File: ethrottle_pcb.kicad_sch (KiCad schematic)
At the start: 52 parts, among them J1 ATM15-08PA-BM02, K1 DIP12-1C90-51x, U1 LM4040DBZ-5, U2 LM324, U3 LM324, U4 LM358_DFN

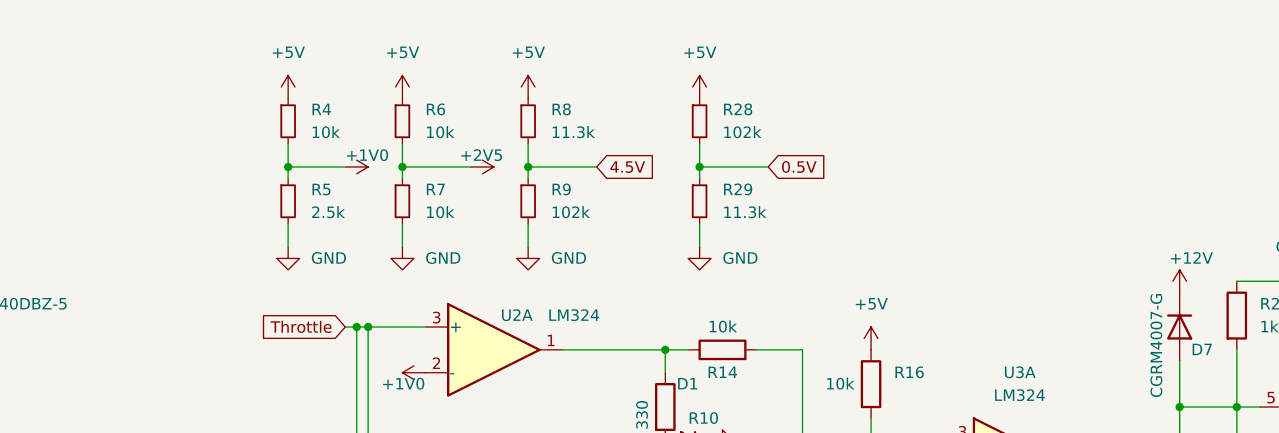
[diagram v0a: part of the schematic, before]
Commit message: add potentiometer
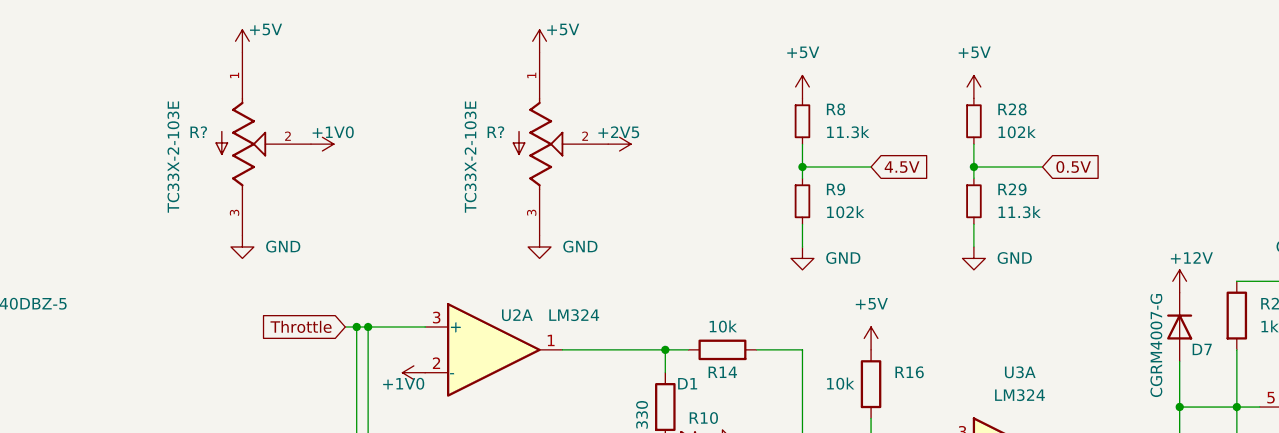
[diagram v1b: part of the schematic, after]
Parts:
- removed R4, R6, R7: 10k, Resistor_SMD:R_01005_0402Metric, symbol Device:R_Small
- removed R5: 2.5k, Resistor_SMD:R_01005_0402Metric, symbol Device:R_Small
- added R? (x2): TC33X-2-103E, TC33X-2-103E:TRIM_TC33X-2-103E, symbol TC33X-2-103E:TC33X-2-103E
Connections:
- net +1V0: now also R?.2
- net +2V5: now also R?.2
- net +5V: now also R?.1, R?.1
- net GND: now also R?.3, R?.3
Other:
- moved on the sheet: R28, R29, R8, R9

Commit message: add TREF/BREF
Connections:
- net +1V0: no longer R?.2, U2.2 (-)
- net +2V5: no longer R?.2, U2.6 (-)
- new net BREF: R?.2, U2.6 (-)
- new net TREF: R?.2, U2.2 (-)
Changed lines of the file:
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@@
+    )
+  )
+  (global_label "BREF" (shape input) (at 97.79 26.67 0) (fields_autoplaced)
+    (effects (font (size 1.27 1.27)) (justify left))
+    (property "Intersheet References" "${INTERSHEET_REFS}" (id 0) (at 104.9807 26.5906 0)
+      (effects (font (size 1.27 1.27)) (justify left) hide)
+    )
+  )
+  (global_label "BREF" (shape input) (at 77.47 71.12 180) (fields_autoplaced)
+    (effects (font (size 1.27 1.27)) (justify right))
+    (property "Intersheet References" "${INTERSHEET_REFS}" (id 0) (at 70.2793 71.1994 0)
+      (effects (font (size 1.27 1.27)) (justify right) hide)
     )
   )
@@
     )
   )
+  (global_label "TREF" (shape input) (at 64.77 26.67 0) (fields_autoplaced)
+    (effects (font (size 1.27 1.27)) (justify left))
+    (property "Intersheet References" "${INTERSHEET_REFS}" (id 0) (at 71.6583 26.5906 0)
+      (effects (font (size 1.27 1.27)) (justify left) hide)
+    )
+  )
   (global_label "4.5V" (shape input) (at 127 29.21 0) (fields_autoplaced)
     (effects (font (size 1.27 1.27)) (justify left))
@@
     )
   )
+  (global_label "TREF" (shape input) (at 77.47 52.07 180) (fields_autoplaced)
+    (effects (font (size 1.27 1.27)) (justify right))
+    (property "Intersheet References" "${INTERSHEET_REFS}" (id 0) (at 70.5817 52.1494 0)
+      (effects (font (size 1.27 1.27)) (justify right) hide)
+    )
+  )
   (global_label "Brake" (shape input) (at 63.5 66.04 180) (fields_autoplaced)
     (effects (font (size 1.27 1.27)) (justify right))
@@
     (pin "1")
     (pin "2")
-  )
-  (symbol (lib_id "power:+1V0") (at 77.47 52.07 90) (unit 1)
-    (in_bom yes) (on_board yes)
-    (property "Reference" "#PWR0110" (id 0) (at 81.28 52.07 0)
-      (effects (font (size 1.27 1.27)) hide)
-    )
-    (property "Value" "+1V0" (id 1) (at 77.47 53.34 90)
-      (effects (font (size 1.27 1.27)) (justify left))
-    )
-    (property "Footprint" "" (id 2) (at 77.47 52.07 0)
-      (effects (font (size 1.27 1.27)) hide)
-    )
-    (property "Datasheet" "" (id 3) (at 77.47 52.07 0)
-      (effects (font (size 1.27 1.27)) hide)
-    )
-    (pin "1")
   )
   (symbol (lib_id "power:+12V") (at 113.03 185.42 180) (unit 1)
@@
     (pin "1")
   )
-  (symbol (lib_id "power:+2V5") (at 77.47 71.12 90) (unit 1)
-    (in_bom yes) (on_board yes) (fields_autoplaced)
-    (property "Reference" "#PWR0115" (id 0) (at 81.28 71.12 0)
-      (effects (font (size 1.27 1.27)) hide)
-    )
-    (property "Value" "+2V5" (id 1) (at 73.66 71.1199 90)
-      (effects (font (size 1.27 1.27)) (justify left))
-    )
-    (property "Footprint" "" (id 2) (at 77.47 71.12 0)
-      (effects (font (size 1.27 1.27)) hide)
-    )
-    (property "Datasheet" "" (id 3) (at 77.47 71.12 0)
-      (effects (font (size 1.27 1.27)) hide)
-    )
-    (pin "1")
-  )
   (symbol (lib_id "power:PWR_FLAG") (at 101.6 181.61 0) (unit 1)
     (in_bom yes) (on_board yes) (fields_autoplaced)
@@
     (pin "1")
   )
-  (symbol (lib_id "power:+1V0") (at 64.77 26.67 270) (unit 1)
-    (in_bom yes) (on_board yes)
-    (property "Reference" "#PWR0107" (id 0) (at 60.96 26.67 0)
-      (effects (font (size 1.27 1.27)) hide)
-    )
-    (property "Value" "+1V0" (id 1) (at 64.77 25.4 90)
-      (effects (font (size 1.27 1.27)) (justify left))
-    )
-    (property "Footprint" "" (id 2) (at 64.77 26.67 0)
-      (effects (font (size 1.27 1.27)) hide)
-    )
-    (property "Datasheet" "" (id 3) (at 64.77 26.67 0)
-      (effects (font (size 1.27 1.27)) hide)
-    )
-    (pin "1")
-  )
   (symbol (lib_id "Relay:DIPxx-1Cxx-51x") (at 243.84 104.14 180) (unit 1)
     (in_bom yes) (on_board yes) (fields_autoplaced)
@@
     (pin "1")
   )
-  (symbol (lib_id "power:+2V5") (at 97.79 26.67 270) (unit 1)
-    (in_bom yes) (on_board yes)
-    (property "Reference" "#PWR0114" (id 0) (at 93.98 26.67 0)
-      (effects (font (size 1.27 1.27)) hide)
-    )
-    (property "Value" "+2V5" (id 1) (at 96.52 25.4 90)
-      (effects (font (size 1.27 1.27)) (justify left))
-    )
-    (property "Footprint" "" (id 2) (at 97.79 26.67 0)
-      (effects (font (size 1.27 1.27)) hide)
-    )
-    (property "Datasheet" "" (id 3) (at 97.79 26.67 0)
-      (effects (font (size 1.27 1.27)) hide)
-    )
-    (pin "1")
-  )
   (symbol (lib_id "Amplifier_Operational:LM324") (at 85.09 111.76 0) (unit 4)
     (in_bom yes) (on_board yes)
@@
       (reference "#PWR0106") (unit 1) (value "+5V") (footprint "")
     )
-    (path "/c3e778b7-a13e-43f0-a5dd-72763097740e"
-      (reference "#PWR0107") (unit 1) (value "+1V0") (footprint "")
-    )
     (path "/0738d770-1a97-45e3-9338-73381352bbbb"
       (reference "#PWR0108") (unit 1) (value "+5V") (footprint "")
@@
       (reference "#PWR0109") (unit 1) (value "+5V") (footprint "")
     )
-    (path "/03fa9d34-f64f-43e8-86a7-eda65b240e1d"
-      (reference "#PWR0110") (unit 1) (value "+1V0") (footprint "")
-    )
     (path "/1fb13a77-46a4-4d35-aa2a-4620ab249d47"
       (reference "#PWR0111") (unit 1) (value "+5V") (footprint "")
@@
       (reference "#PWR0113") (unit 1) (value "GND") (footprint "")
     )
-    (path "/d9e3bb88-8693-4e36-af80-732a6a16d6f2"
-      (reference "#PWR0114") (unit 1) (value "+2V5") (footprint "")
-    )
-    (path "/605db75b-88d9-4f7e-b98f-01a708aff33d"
-      (reference "#PWR0115") (unit 1) (value "+2V5") (footprint "")
-    )
     (path "/f0d8fdd2-cc4f-4bf1-ba1a-b6fce7e98272"

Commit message: adjust layout
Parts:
- gave numbers to parts that had none: 2
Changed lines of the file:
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@@
   (symbol (lib_id "power:+5V") (at 57.15 16.51 0) (unit 1)
     (in_bom yes) (on_board yes)
-    (property "Reference" "#PWR?" (id 0) (at 57.15 20.32 0)
+    (property "Reference" "#PWR0101" (id 0) (at 57.15 20.32 0)
       (effects (font (size 1.27 1.27)) hide)
     )
@@
   (symbol (lib_id "power:+5V") (at 90.17 16.51 0) (unit 1)
     (in_bom yes) (on_board yes)
-    (property "Reference" "#PWR?" (id 0) (at 90.17 20.32 0)
+    (property "Reference" "#PWR0103" (id 0) (at 90.17 20.32 0)
       (effects (font (size 1.27 1.27)) hide)
     )
@@
   (symbol (lib_id "TC33X-2-103E:TC33X-2-103E") (at 57.15 26.67 270) (unit 1)
     (in_bom yes) (on_board yes)
-    (property "Reference" "R?" (id 0) (at 53.34 25.3999 90)
+    (property "Reference" "R4" (id 0) (at 53.34 25.3999 90)
       (effects (font (size 1.27 1.27)) (justify right))
     )
@@
   (symbol (lib_id "TC33X-2-103E:TC33X-2-103E") (at 90.17 26.67 270) (unit 1)
     (in_bom yes) (on_board yes)
-    (property "Reference" "R?" (id 0) (at 86.36 25.3999 90)
+    (property "Reference" "R5" (id 0) (at 86.36 25.3999 90)
       (effects (font (size 1.27 1.27)) (justify right))
     )
@@
   (symbol (lib_id "power:GND") (at 90.17 36.83 0) (unit 1)
     (in_bom yes) (on_board yes) (fields_autoplaced)
-    (property "Reference" "#PWR?" (id 0) (at 90.17 43.18 0)
+    (property "Reference" "#PWR0104" (id 0) (at 90.17 43.18 0)
       (effects (font (size 1.27 1.27)) hide)
     )
@@
       (reference "#PWR033") (unit 1) (value "GND") (footprint "")
     )
+    (path "/0b28ad2f-122c-46f1-b095-f0acacd460ac"
+      (reference "#PWR0101") (unit 1) (value "+5V") (footprint "")
+    )
     (path "/f1df09a9-e714-4783-9999-ec6ab2809683"
       (reference "#PWR0102") (unit 1) (value "+5V") (footprint "")
     )
+    (path "/7cac6d18-b1ff-4158-927b-4a7afa7e306a"
+      (reference "#PWR0103") (unit 1) (value "+5V") (footprint "")
+    )
+    (path "/ecda5c0c-7556-4038-b147-690988ab17da"
+      (reference "#PWR0104") (unit 1) (value "GND") (footprint "")
+    )
     (path "/c5eaef10-b497-4e30-9734-8f1cebcdc9de"
       (reference "#PWR0105") (unit 1) (value "+1V0") (footprint "")
@@
       (reference "#PWR0116") (unit 1) (value "+2V5") (footprint "")
     )
-    (path "/0b28ad2f-122c-46f1-b095-f0acacd460ac"
-      (reference "#PWR?") (unit 1) (value "+5V") (footprint "")
-    )
-    (path "/7cac6d18-b1ff-4158-927b-4a7afa7e306a"
-      (reference "#PWR?") (unit 1) (value "+5V") (footprint "")
-    )
-    (path "/ecda5c0c-7556-4038-b147-690988ab17da"
-      (reference "#PWR?") (unit 1) (value "GND") (footprint "")
-    )
     (path "/9693536b-4727-4111-bd6e-6b5a38100334"
       (reference "C1") (unit 1) (value "10uF") (footprint "Capacitor_SMD:C_0805_2012Metric")
@@
       (reference "R3") (unit 1) (value "100k") (footprint "Resistor_SMD:R_01005_0402Metric")
     )
+    (path "/9abae127-e0ee-46b2-b6e2-dbc096437d9a"
+      (reference "R4") (unit 1) (value "TC33X-2-103E") (footprint "TC33X-2-103E:TRIM_TC33X-2-103E")
+    )
+    (path "/ce087a79-088a-4b36-9551-61344a061170"
+      (reference "R5") (unit 1) (value "TC33X-2-103E") (footprint "TC33X-2-103E:TRIM_TC33X-2-103E")
+    )
     (path "/f9c8b0cc-aaac-4839-834f-a2ce216cbb8f"
       (reference "R8") (unit 1) (value "11.3k") (footprint "Resistor_SMD:R_01005_0402Metric")
@@
       (reference "R29") (unit 1) (value "11.3k") (footprint "Resistor_SMD:R_01005_0402Metric")
     )
-    (path "/9abae127-e0ee-46b2-b6e2-dbc096437d9a"
-      (reference "R?") (unit 1) (value "TC33X-2-103E") (footprint "TC33X-2-103E:TRIM_TC33X-2-103E")
-    )
-    (path "/ce087a79-088a-4b36-9551-61344a061170"
-      (reference "R?") (unit 1) (value "TC33X-2-103E") (footprint "TC33X-2-103E:TRIM_TC33X-2-103E")
-    )
     (path "/308d6a19-13d9-4a79-af04-65baedb82d13"

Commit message: update constraints & layout
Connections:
- net Brake: now also J1.3; no longer J1.4
- net GND: now also J1.4, J1.MH1, J1.MH2, J1.MH3, J1.MH4; no longer J1.2, J1.6
- net Throttle: now also J1.2; no longer J1.3
- net Output: no longer names the net of J1.5
- net Output: no longer K1.1

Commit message: fills & routing
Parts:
- removed K1: DIP12-1C90-51x, Relay_THT:Relay_StandexMeder_DIP_LowProfile, symbol Relay:DIPxx-1Cxx-51x
- added K1: 1462042-9, ul_1462042-9:1462042-9, symbol UL_relay:1462042-9
- renumbered D15 to D10, D7 to D11, D8 to D12, D9 to D13, D10 to D14, D11 to D15, D12 to D5, D13 to D6, D5 to D7, D6 to D8, D14 to D9, R12 to R10, R13 to R11, R26 to R12, R27 to R13, R8 to R16, R9 to R17, R16 to R18, R17 to R19, R4 to R2, R18 to R20, R28 to R21, R29 to R22, R19 to R23, R20 to R24, R21 to R25, R22 to R26, R23 to R27, R24 to R3, R25 to R4, R2 to R5, R3 to R6, R5 to R7, R10 to R8, R11 to R9, U4 to U3, U3 to U4
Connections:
- net GND: now also K1.5, K1.8
- net at D15.1 (K): now also K1.3
- net at U4.14: now also K1.1
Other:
- moved on the sheet: D15, R27

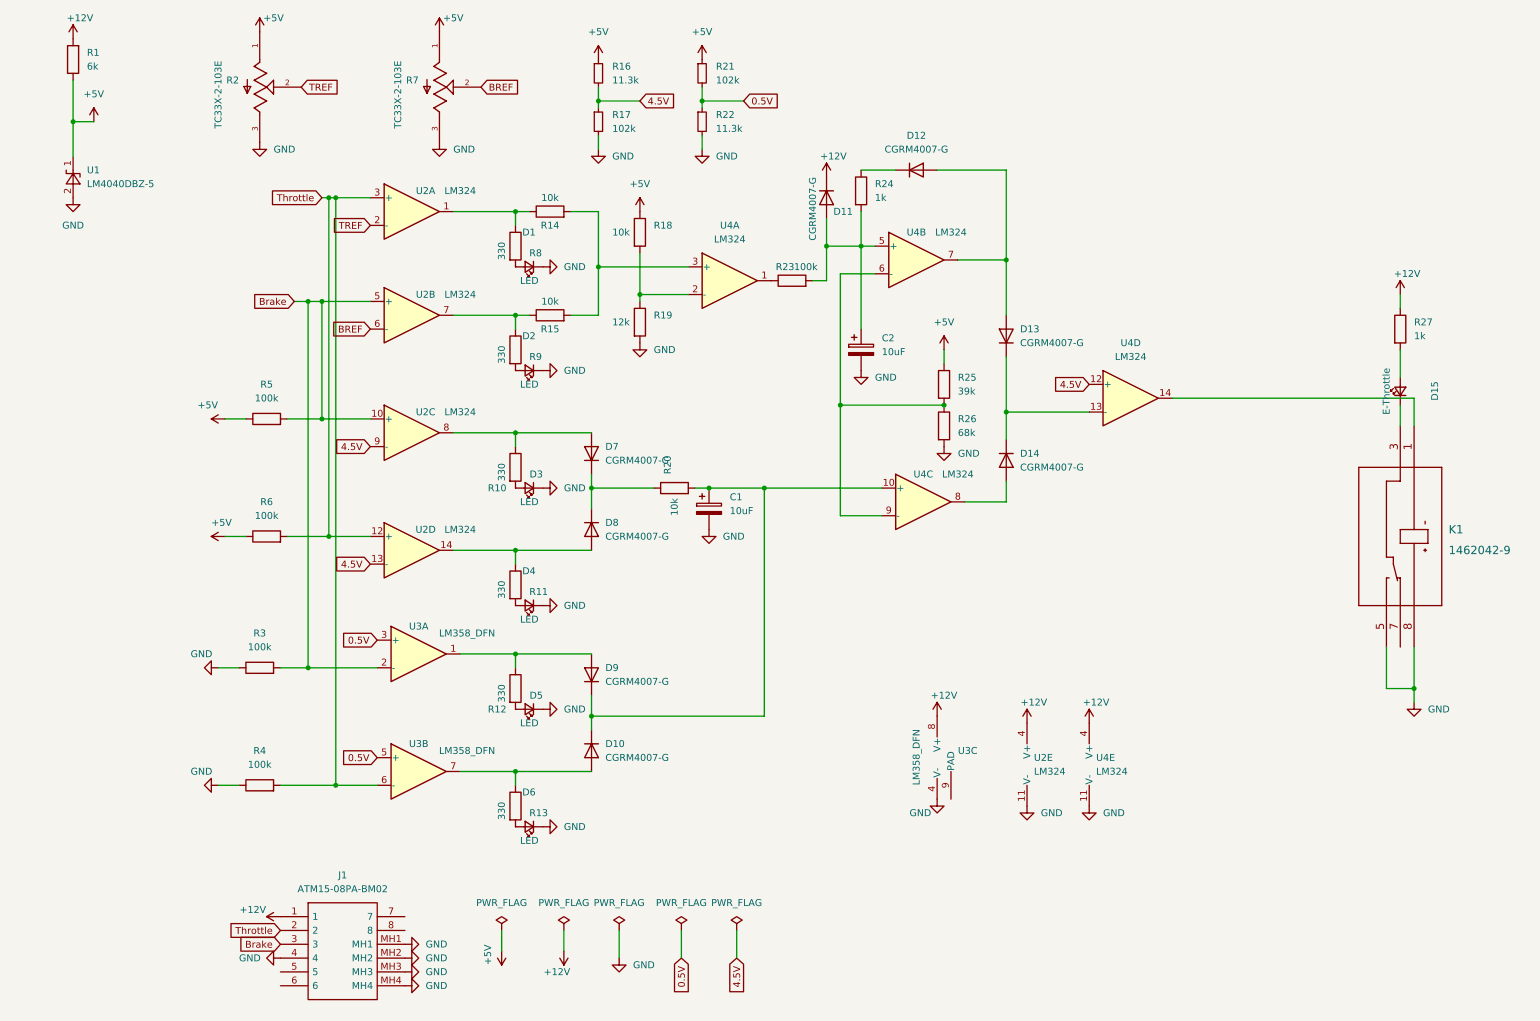
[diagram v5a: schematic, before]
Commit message: updated schematic, not pcb
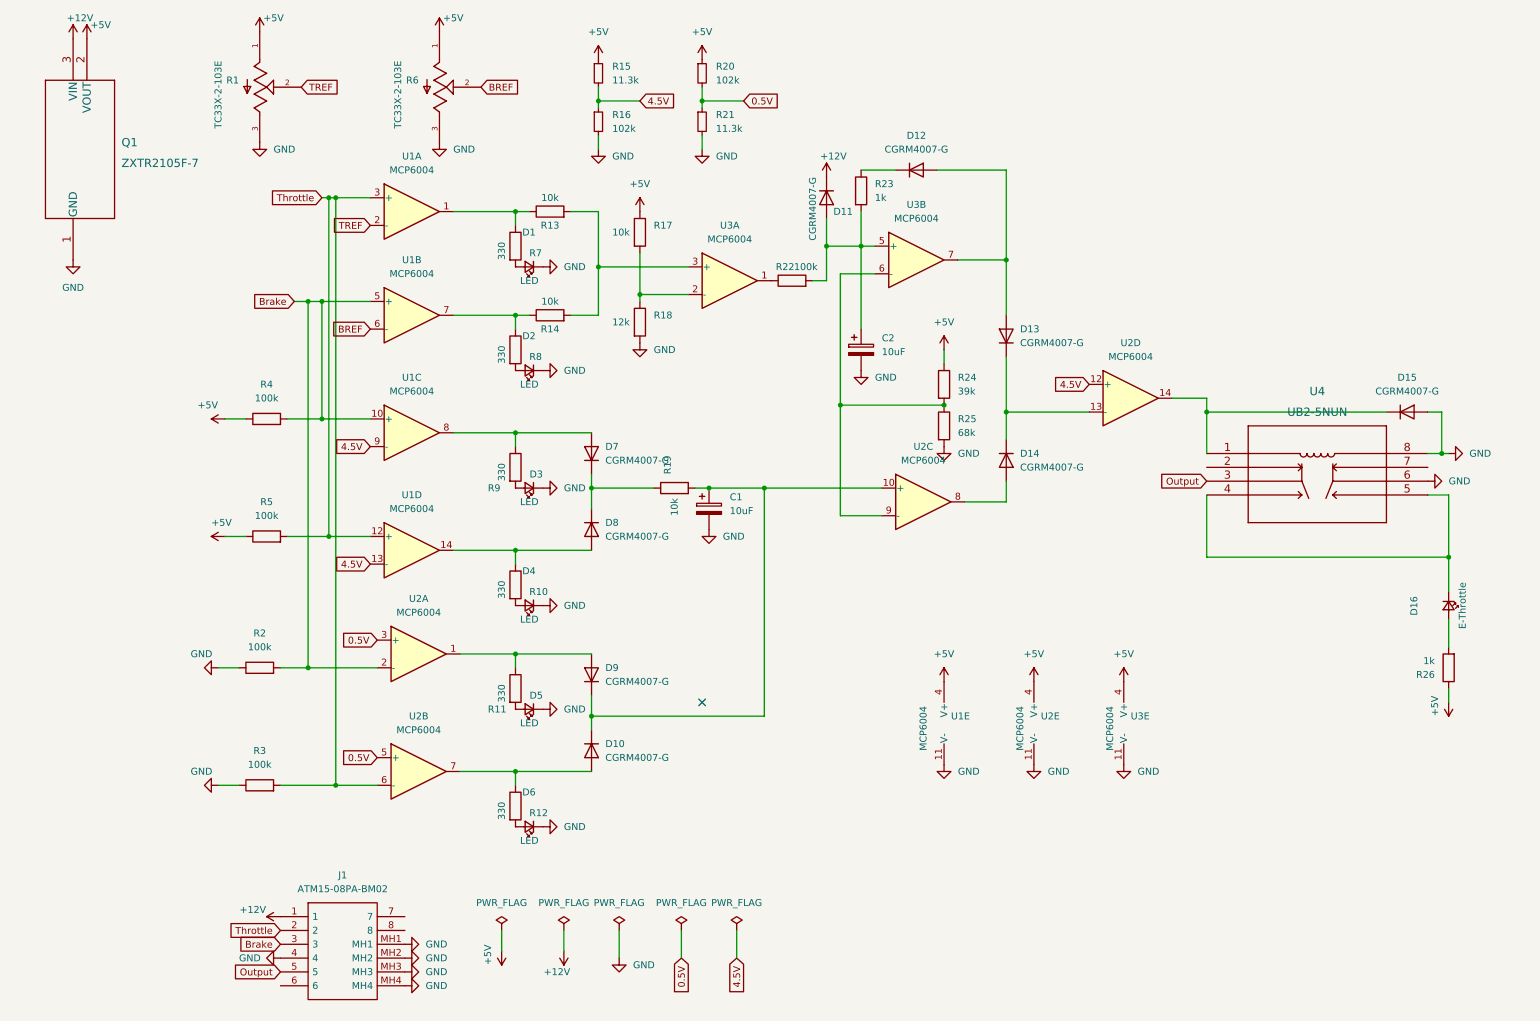
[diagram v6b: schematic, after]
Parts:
- removed K1: 1462042-9, ul_1462042-9:1462042-9, symbol UL_relay:1462042-9
- removed R1: 6k, Resistor_SMD:R_01005_0402Metric, symbol Device:R
- removed U1: LM4040DBZ-5, Package_TO_SOT_SMD:SOT-23, symbol Reference_Voltage:LM4040DBZ-5
- removed U2, U4: LM324, LM324PWR:LM324PWR, symbol Amplifier_Operational:LM324
- removed U3: LM358_DFN, Package_DFN_QFN:DFN-8-1EP_2x2mm_P0.5mm_EP1.05x1.75mm, symbol Amplifier_Operational:LM358_DFN
- added D15: CGRM4007-G, Diode_SMD:D_SOD-123, symbol Diode:1N5401
- added Q1: ZXTR2105F-7, ZXTR2105F-7:ZXTR2105F-7, symbol ZXTR2105F-7:ZXTR2105F-7
- added U1, U2, U3: MCP6004, MCP6004T-I_ST:SOP65P640X120-14N, symbol Amplifier_Operational:MCP6004
- added U4: UB2-5NUN, UB2-5NUN:UB2-5NUN, symbol UB2-5NUN:UB2-5NUN
- renumbered D15 to D16, R2 to R1, R11 to R10, R12 to R11, R13 to R12, R14 to R13, R15 to R14, R16 to R15, R17 to R16, R18 to R17, R19 to R18, R20 to R19, R3 to R2, R21 to R20, R22 to R21, R23 to R22, R24 to R23, R25 to R24, R26 to R25, R27 to R26, R4 to R3, R5 to R4, R6 to R5, R7 to R6, R8 to R7, R9 to R8, R10 to R9
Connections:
- net +12V: now also Q1.3 (VIN); no longer R26.1
- net +5V: now also R26.1, Q1.2 (VOUT), U1.4 (V+), U2.4 (V+), U3.4 (V+)
- net 0.5V: now also U2.3 (+), U2.5 (+)
- net 4.5V: now also U1.13 (-), U1.9 (-), U2.12 (+)
- net BREF: now also U1.6 (-)
- net Brake: now also U1.10 (+), U1.5 (+), U2.2 (-)
- net GND: now also D15.2 (A), Q1.1 (GND), U1.11 (V-), U2.11 (V-), U3.11 (V-), U4.6, U4.8
- net TREF: now also U1.2 (-)
- net Throttle: now also U1.12 (+), U1.3 (+), U2.6 (-)
- net at D7.2 (A), R9.1: now also U1.8
- net at R13.1, R7.1: now also U1.1
- net at D10.2 (A), R12.1: now also U2.7
- net at R24.2, R25.1: now also U2.9 (-), U3.6 (-)
- net at D13.1 (K), D14.1 (K): now also U2.13 (-)
- net at D12.2 (A), D13.2 (A): now also U3.7
- net at R17.2, R18.1: now also U3.2 (-)
- net at R22.1: now also U3.1
- net at R13.2, R14.2: now also U3.3 (+)
- net at C2.1, D11.2 (A), R22.2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: now also U3.5 (+)
- net at R14.1, R8.1: now also U1.7
- net Output: now reaches J1.5
- net Output: now also U4.3
- net at D16.1 (K): now also U4.4, U4.5
- net at D14.2 (A): now also U2.8
- net at C1.1, D10.1 (K), D9.1 (K)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: now also U2.10 (+)
- net at D9.2 (A), R11.1: now also U2.1
- net at D8.2 (A), R10.1: now also U1.14
- new net: D15.1 (K), U2.14, U4.1
- no-connect marks 0 -> 1
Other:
- moved on the sheet: D16, R26

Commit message: layout changes
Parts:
- added C? (x3): 100nF, Capacitor_SMD:C_0201_0603Metric, symbol Device:C_Small
- added H? (x4): MountingHole_Pad, symbol Mechanical:MountingHole_Pad
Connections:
- net +12V: now also R26.1, U4.4, U4.5
- net +5V: now also C?.1, C?.1, C?.1; no longer R26.1
- net GND: now also D16.1 (K), C?.2, C?.2, C?.2, H?.1, H?.1, H?.1, H?.1; no longer U4.6
- net Output: now also U4.2, U4.6, U4.7
- no-connect marks 1 -> 0
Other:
- moved on the sheet: C1, C2, D1, D10, D11, D12, D13, D14, D15, D16, D2, D3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

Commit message: updates
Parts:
- gave numbers to parts that had none: 7
- renumbered C1 to C2, C2 to C5, D16 to D15, D15 to D16
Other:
- moved on the sheet: Q1
